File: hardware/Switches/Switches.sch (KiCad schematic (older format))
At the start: 22 parts, among them U101 MIC4604YM, U102 MIC4604YM

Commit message: snubber
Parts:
- added C105, C106, C107, C108: 100n, Capacitor_SMD:C_1210_3225Metric_Pad1.33x2.70mm_HandSolder, symbol Device:C_Small
- added R109, R110, R111, R112: 10, Resistor_SMD:R_1210_3225Metric_Pad1.30x2.65mm_HandSolder, symbol Device:R_Small_US
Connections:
- wire segments 71 -> 75
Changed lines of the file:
@@
 	5950 3950 5800 3950
 Wire Wire Line
-	6100 4350 5800 4350
-Wire Wire Line
-	3850 4350 4150 4350
+	6100 4350 5950 4350
+Wire Wire Line
+	3850 4350 4000 4350
 Wire Wire Line
 	5800 4350 4950 4350
@@
 Connection ~ 4150 4350
 Wire Wire Line
-	3850 2650 4150 2650
+	3850 2650 4000 2650
 Connection ~ 4150 2650
 Wire Wire Line
@@
 Connection ~ 5800 2650
 Wire Wire Line
-	5800 2650 6100 2650
+	5800 2650 5950 2650
 Wire Wire Line
 	4000 3550 4600 3550
@@
 Wire Wire Line
 	1400 4000 1400 4250
+$Comp
+L Device:R_Small_US R109
+U 1 1 606721D1
+P 4000 2750
+F 0 "R109" V 4050 2650 50  0000 C CNN
+F 1 "10" V 3800 2850 50  0000 C CNN
+F 2 "Resistor_SMD:R_1210_3225Metric_Pad1.30x2.65mm_HandSolder" H 4000 2750 50  0001 C CNN
+F 3 "~" H 4000 2750 50  0001 C CNN
+	1    4000 2750
+	1    0    0    1
+$EndComp
+Connection ~ 4000 2650
+Wire Wire Line
+	4000 2650 4150 2650
+$Comp
+L Device:C_Small C105
+U 1 1 606739D1
+P 4000 2950
+F 0 "C105" H 4092 2996 50  0000 L CNN
+F 1 "100n" H 4092 2905 50  0000 L CNN
+F 2 "Capacitor_SMD:C_1210_3225Metric_Pad1.33x2.70mm_HandSolder" H 4000 2950 50  0001 C CNN
+F 3 "~" H 4000 2950 50  0001 C CNN
+	1    4000 2950
+	1    0    0    -1
+$EndComp
+$Comp
+L Device:R_Small_US R111
+U 1 1 60674F65
+P 5950 2750
+F 0 "R111" V 6000 2650 50  0000 C CNN
+F 1 "10" V 5750 2850 50  0000 C CNN
+F 2 "Resistor_SMD:R_1210_3225Metric_Pad1.30x2.65mm_HandSolder" H 5950 2750 50  0001 C CNN
+F 3 "~" H 5950 2750 50  0001 C CNN
+	1    5950 2750
+	1    0    0    1
+$EndComp
+Connection ~ 5950 2650
+Wire Wire Line
+	5950 2650 6100 2650
+$Comp
+L Device:C_Small C107
+U 1 1 606754F2
+P 5950 2950
+F 0 "C107" H 6042 2996 50  0000 L CNN
+F 1 "100n" H 6042 2905 50  0000 L CNN
+F 2 "Capacitor_SMD:C_1210_3225Metric_Pad1.33x2.70mm_HandSolder" H 5950 2950 50  0001 C CNN
+F 3 "~" H 5950 2950 50  0001 C CNN
+	1    5950 2950
+	1    0    0    -1
+$EndComp
+$Comp
+L Device:R_Small_US R110
+U 1 1 6067713F
+P 4000 4050
+F 0 "R110" V 4050 3950 50  0000 C CNN
+F 1 "10" V 3800 4150 50  0000 C CNN
+F 2 "Resistor_SMD:R_1210_3225Metric_Pad1.30x2.65mm_HandSolder" H 4000 4050 50  0001 C CNN
+F 3 "~" H 4000 4050 50  0001 C CNN
+	1    4000 4050
+	1    0    0    1
+$EndComp
+$Comp
+L Device:C_Small C106
+U 1 1 6067937E
+P 4000 4250
+F 0 "C106" H 4092 4296 50  0000 L CNN
+F 1 "100n" H 4092 4205 50  0000 L CNN
+F 2 "Capacitor_SMD:C_1210_3225Metric_Pad1.33x2.70mm_HandSolder" H 4000 4250 50  0001 C CNN
+F 3 "~" H 4000 4250 50  0001 C CNN
+	1    4000 4250
+	1    0    0    -1
+$EndComp
+Connection ~ 4000 4350
+Wire Wire Line
+	4000 4350 4150 4350
+$Comp
+L Device:R_Small_US R112
+U 1 1 6067A27F
+P 5950 4050
+F 0 "R112" V 6000 3950 50  0000 C CNN
+F 1 "10" V 5750 4150 50  0000 C CNN
+F 2 "Resistor_SMD:R_1210_3225Metric_Pad1.30x2.65mm_HandSolder" H 5950 4050 50  0001 C CNN
+F 3 "~" H 5950 4050 50  0001 C CNN
+	1    5950 4050
+	1    0    0    1
+$EndComp
+$Comp
+L Device:C_Small C108
+U 1 1 6067A8BA
+P 5950 4250
+F 0 "C108" H 6042 4296 50  0000 L CNN
+F 1 "100n" H 6042 4205 50  0000 L CNN
+F 2 "Capacitor_SMD:C_1210_3225Metric_Pad1.33x2.70mm_HandSolder" H 5950 4250 50  0001 C CNN
+F 3 "~" H 5950 4250 50  0001 C CNN
+	1    5950 4250
+	1    0    0    -1
+$EndComp
+Connection ~ 5950 4350
+Wire Wire Line
+	5950 4350 5800 4350
 $EndSCHEMATC

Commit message: wip: switches pcb routed
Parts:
- removed C101, C104: 100n, Capacitor_SMD:C_0805_2012Metric_Pad1.18x1.45mm_HandSolder, symbol Device:C_Small
- removed C105: 100n, Capacitor_SMD:C_1210_3225Metric_Pad1.33x2.70mm_HandSolder, symbol Device:C_Small
- removed QH1_1, QH1_2, QH2_1, QH2_2, QL1_1, QL1_2, QL2_1, QL2_2: IAUT300N10S5N015, Package_TO_SOT_SMD:Infineon_PG-HSOF-8-1, symbol Device:Q_NMOS_GSD
- removed R109: 10, Resistor_SMD:R_1210_3225Metric_Pad1.30x2.65mm_HandSolder, symbol Device:R_Small_US
- removed U101, U102: MIC4604YM, Package_SO:SOIC-8_3.9x4.9mm_P1.27mm, symbol Driver_FET:MIC4604YM
- added C101, C104, C112, C113, C114, C115, C116, C117, C118, C119, C120, C121, C123, C124, C125, C126, C127, C128, C129, C130: 10u, Capacitor_SMD:C_1210_3225Metric_Pad1.33x2.70mm_HandSolder, symbol Device:C
- added C106: 100n, Capacitor_SMD:C_1210_3225Metric_Pad1.33x2.70mm_HandSolder, symbol Device:C_Small
- added C109, C110, C122: 10uF, Capacitor_SMD:C_1210_3225Metric_Pad1.33x2.70mm_HandSolder, symbol Device:C_Small
- added C111: 100nF, Capacitor_SMD:C_0805_2012Metric_Pad1.18x1.45mm_HandSolder, symbol Device:C_Small
- added C131, C132, C133: 1pF, Capacitor_SMD:C_0603_1608Metric_Pad1.08x0.95mm_HandSolder, symbol Device:C_Small
- added C134: 100nF, Capacitor_SMD:C_0603_1608Metric_Pad1.08x0.95mm_HandSolder, symbol Device:C_Small
- added J101, J102, J103, J104: BusBar, Switches:BusBar, symbol Connector:Conn_01x01_Male
- added J105: Conn_02x03_Odd_Even, Connector_PinHeader_1.27mm:PinHeader_2x10_P1.27mm_Vertical_SMD, symbol Connector_Generic:Conn_02x10_Odd_Even
- added Q101, Q102, Q103, Q104, Q105, Q106, Q107, Q108, Q109, Q110, Q111, Q112: IPT015N10N5, Package_TO_SOT_SMD:Infineon_PG-HSOF-8-1_ThermalVias, symbol Transistor_FET:IPT015N10N5
- added R110: 10, Resistor_SMD:R_1210_3225Metric_Pad1.30x2.65mm_HandSolder, symbol Device:R_Small_US
- added R113, R114, R115, R116: 4R7, Resistor_SMD:R_0805_2012Metric_Pad1.20x1.40mm_HandSolder, symbol Device:R_Small_US
- added R117: 47k, Resistor_SMD:R_0603_1608Metric_Pad0.98x0.95mm_HandSolder, symbol Device:R_Small_US
- added R118, R119, R120, R124, R125, R126, R127, R128, R129, R130, R131, R132, R133, R134, R135: 10k, Resistor_SMD:R_0603_1608Metric_Pad0.98x0.95mm_HandSolder, symbol Device:R_Small_US
- added R121, R122, R123: 330, Resistor_SMD:R_0603_1608Metric_Pad0.98x0.95mm_HandSolder, symbol Device:R_Small_US
- added TH101: SDNT2012X103F3950FTF, Resistor_SMD:R_0805_2012Metric_Pad1.20x1.40mm_HandSolder, symbol Device:Thermistor_NTC_US
- added U101, U102: UCC27211DDAR, Package_SO:SOIC-8-1EP_3.9x4.9mm_P1.27mm_EP2.514x3.2mm_ThermalVias, symbol ucc27211ddar:UCC27211DDAR
- C102, C103: footprint Capacitor_SMD:C_0805_2012Metric_Pad1.18x1.45mm_HandSolder -> Capacitor_SMD:C_1210_3225Metric_Pad1.33x2.70mm_HandSolder
- C107: value 100n -> 10uF
- C108: value 100n -> 100nF; footprint Capacitor_SMD:C_1210_3225Metric_Pad1.33x2.70mm_HandSolder -> Capacitor_SMD:C_0805_2012Metric_Pad1.18x1.45mm_HandSolder
- R101, R102: footprint Resistor_SMD:R_0805_2012Metric_Pad1.20x1.40mm_HandSolder -> Resistor_SMD:R_1210_3225Metric_Pad1.30x2.65mm_HandSolder
- R103, R104, R105, R106, R107, R108: value 10 -> 4R7
- R111, R112: value 10 -> 4R7; footprint Resistor_SMD:R_1210_3225Metric_Pad1.30x2.65mm_HandSolder -> Resistor_SMD:R_0805_2012Metric_Pad1.20x1.40mm_HandSolder
- renumbered C106 to C105, R110 to R109
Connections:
- net labels added: +15V, +BATT, GH1_3, GH2_3, GL1_3, GL3_3, GNDA, PWM_H1, PWM_H2, PWM_L1, PWM_L2, SL1_sen, SL2_sen, TEMP1, Vin_sen
- net labels removed: VCC, Vin
- wire segments 75 -> 325
- no-connect marks 0 -> 6
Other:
- note added: "References:\nhttps://www.ti.com/lit/an/slva959a/slva959a.pdf\nhttps://www.ti.com/tool/TIDA-00774"
- note added: "TODO:\n [_] Definir fixação no dissipador!!!!!!!!\n [_] Calcular capacitores do Driver!\n [x] Incluir sensores de tensão\n [x] Incluir sensores de temperatura\n [_] Incluir diodo no Snubber\n [_] Usar plano em baixo da barra de cobre para aumentar a capacitância de entrada\n [_] Verificar pinagem no conector do controle\n [_] Calcular capacitores de entrada\n [x] Incluir sensores de corrente -> S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"
- note added: "≃12kHz"
- note added: "≃200Hz@25°C\n≃2.7kHz@125°C"
- note removed: "Q1-Q8 IAUT300N10S5N015"
- moved on the sheet: C105, R109

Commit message: Driver and MOSFETs protections added, driver calculations done.
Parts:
- added C135, C136, C137, C138, C139, C140, C141, C142, C143, C144, C145, C146, C147, C148, C149, C150, C151, C152, C153, C154: 100n, Capacitor_SMD:C_0805_2012Metric_Pad1.18x1.45mm_HandSolder, symbol Device:C
- added C155, C156, C157, C158, C159, C160, C161, C162, C163, C164, C165, C166, C167, C168, C169, C170, C171, C172, C173, C174: 10n, Capacitor_SMD:C_0603_1608Metric_Pad1.08x0.95mm_HandSolder, symbol Device:C
- added C175, C176, C177, C178, C179, C180, C181, C182, C183, C184, C185, C186, C187, C188, C189, C190, C191, C192, C193, C194: 1n, Capacitor_SMD:C_0603_1608Metric_Pad1.08x0.95mm_HandSolder, symbol Device:C
- added C195, C196: 1n, Capacitor_SMD:C_0603_1608Metric_Pad1.08x0.95mm_HandSolder, symbol Device:C_Small
- added D101, D103, D104, D105, D106, D107, D108, D109, D111, D112, D113, D115, D116, D117: B0530W, Diode_SMD:D_SOD-123F, symbol Device:D_Schottky_Small
- added D102, D110: MBR2H100SFT3G, Diode_SMD:D_SOD-123F, symbol Device:D_Schottky_Small
- added D114, D118: MM3Z15V, Diode_SMD:D_SOD-323, symbol Device:D_Zener_Small
- added R136, R137: 2R, Resistor_SMD:R_0603_1608Metric_Pad0.98x0.95mm_HandSolder, symbol Device:R_Small_US
- C107, C110: value 10uF -> 10u
- C108, C111, C134: value 100nF -> 100n
- C109, C122: value 10uF -> 4.7u
- C131, C132, C133: value 1pF -> 1p
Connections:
- wire segments 325 -> 617
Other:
- note added: "TODO:\n [_] Definir fixação no dissipador!!!!!!!!\n [x] Calcular capacitores do Driver!\n [x] Incluir sensores de tensão\n [x] Incluir sensores de temperatura\n [_] Incluir diodo no Snubber\n [_] Usar plano em baixo da barra de cobre para aumentar a capacitância de entrada\n [_] Verificar pinagem no conector do controle\n [_] Calcular capacitores de entrada\n [x] Incluir sensores de corrente -> S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"
- note removed: "TODO:\n [_] Definir fixação no dissipador!!!!!!!!\n [_] Calcular capacitores do Driver!\n [x] Incluir sensores de tensão\n [x] Incluir sensores de temperatura\n [_] Incluir diodo no Snubber\n [_] Usar plano em baixo da barra de cobre para aumentar a capacitância de entrada\n [_] Verificar pinagem no conector do controle\n [_] Calcular capacitores de entrada\n [x] Incluir sensores de corrente -> S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"
- moved on the sheet: C101, C102, C103, C104, C105, C106, C107, C108, C109, C110, C111, C112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

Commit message: wip: PCB updated
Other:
- note added: "References:\nhttps://www.ti.com/lit/an/slva959a/slva959a.pdf\nhttps://www.ti.com/tool/TIDA-00774\nhttps://www.ti.com/lit/ug/tiducb6/tiducb6.pdf"
- note removed: "References:\nhttps://www.ti.com/lit/an/slva959a/slva959a.pdf\nhttps://www.ti.com/tool/TIDA-00774"

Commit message: Updating Switches PCB
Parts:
- R117: value 47k -> 5k6
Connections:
- net labels added: +5VA
- wire segments 617 -> 624
- no-connect marks 6 -> 0
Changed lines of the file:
@@
 	0    1    1    0
 $EndComp
-Text Label 3150 2550 0    50   ~ 0
+Text Label 3150 2650 0    50   ~ 0
 PWM_H1
-Text Label 3150 2450 0    50   ~ 0
+Text Label 3150 2550 0    50   ~ 0
 PWM_L1
-Text Label 3150 2750 0    50   ~ 0
+Text Label 3150 2850 0    50   ~ 0
 PWM_H2
-Text Label 3150 2650 0    50   ~ 0
+Text Label 3150 2750 0    50   ~ 0
 PWM_L2
 $Comp
 L power:+15V #PWR0101
 U 1 1 60920038
-P 3150 1600
-F 0 "#PWR0101" H 3150 1450 50  0001 C CNN
-F 1 "+15V" H 3150 1800 50  0000 C CNN
-F 2 "" H 3150 1600 50  0001 C CNN
-F 3 "" H 3150 1600 50  0001 C CNN
-	1    3150 1600
+P 4100 2000
+F 0 "#PWR0101" H 4100 1850 50  0001 C CNN
+F 1 "+15V" H 4100 2200 50  0000 C CNN
+F 2 "" H 4100 2000 50  0001 C CNN
+F 3 "" H 4100 2000 50  0001 C CNN
+	1    4100 2000
 	1    0    0    -1
 $EndComp
 Wire Wire Line
-	3150 1600 3150 1650
+	4100 2000 4100 2050
 Wire Wire Line
 	3150 2050 3050 2050
-Connection ~ 3150 1650
-Wire Wire Line
-	3150 1650 3150 2050
 $Comp
 L Device:C_Small C111
@@
 L power:PWR_FLAG #FLG0101
 U 1 1 60CF3365
-P 2800 1650
-F 0 "#FLG0101" H 2800 1725 50  0001 C CNN
-F 1 "PWR_FLAG" H 2800 1850 50  0000 C CNN
-F 2 "" H 2800 1650 50  0001 C CNN
-F 3 "~" H 2800 1650 50  0001 C CNN
-	1    2800 1650
+P 3750 2050
+F 0 "#FLG0101" H 3750 2125 50  0001 C CNN
+F 1 "PWR_FLAG" H 3750 2250 50  0000 C CNN
+F 2 "" H 3750 2050 50  0001 C CNN
+F 3 "~" H 3750 2050 50  0001 C CNN
+	1    3750 2050
 	1    0    0    -1
 $EndComp
 Wire Wire Line
-	2800 1650 3150 1650
-NoConn ~ 2450 2250
-NoConn ~ 2450 2350
-NoConn ~ 3150 2350
-NoConn ~ 3150 2850
-NoConn ~ 3150 2950
-NoConn ~ 3150 2250
+	3750 2050 4100 2050
 Wire Wire Line
 	3150 2850 3050 2850
 Wire Wire Line
-	3150 2950 3050 2950
-Wire Wire Line
 	1500 8200 1500 8000
 Wire Wire Line
@@
 Text Notes 9550 11050 0    50   ~ 0
 References:\nhttps://www.ti.com/lit/an/slva959a/slva959a.pdf\nhttps://www.ti.com/tool/TIDA-00774\nhttps://www.ti.com/lit/ug/tiducb6/tiducb6.pdf
-Text Label 2450 2750 2    50   ~ 0
+Text Label 2450 2850 2    50   ~ 0
 TEMP1
 $Comp
@@
 Wire Wire Line
 	7950 2150 7950 2250
-Text Label 2450 2450 2    50   ~ 0
-SL1_sen
 Text Label 2450 2550 2    50   ~ 0
-SL2_sen
+SL1_sen
 Text Label 2450 2650 2    50   ~ 0
+SL2_sen
+Text Label 2450 2750 2    50   ~ 0
 Vin_sen
 $Comp
@@
 P 9600 2350
 F 0 "R117" H 9450 2400 50  0000 C CNN
-F 1 "47k" H 9450 2300 50  0000 C CNN
+F 1 "5k6" H 9450 2300 50  0000 C CNN
 F 2 "Resistor_SMD:R_0603_1608Metric_Pad0.98x0.95mm_HandSolder" H 9600 2350 50  0001 C CNN
 F 3 "~" H 9600 2350 50  0001 C CNN
@@
 	-1   0    0    -1
 $EndComp
-$Comp
-L power:+15V #PWR0113
-U 1 1 60A6701F
-P 9600 2250
-F 0 "#PWR0113" H 9600 2100 50  0001 C CNN
-F 1 "+15V" H 9600 2450 50  0000 C CNN
-F 2 "" H 9600 2250 50  0001 C CNN
-F 3 "" H 9600 2250 50  0001 C CNN
-	1    9600 2250
-	1    0    0    -1
-$EndComp
 Wire Wire Line
 	9600 2500 9600 2550
@@
 $EndComp
 Wire Wire Line
-	1950 2850 1950 2950
-Wire Wire Line
-	1950 2850 2550 2850
-Wire Wire Line
 	1950 2950 2550 2950
 Connection ~ 1950 2950
@@
 Wire Wire Line
 	3150 2150 3150 2050
-Connection ~ 3150 2050
 $Comp
 L power:PWR_FLAG #FLG0104
 U 1 1 6142A2F3
-P 1950 2850
-F 0 "#FLG0104" H 1950 2925 50  0001 C CNN
-F 1 "PWR_FLAG" H 1950 3050 50  0000 C CNN
-F 2 "" H 1950 2850 50  0001 C CNN
-F 3 "~" H 1950 2850 50  0001 C CNN
-	1    1950 2850
+P 1950 2950
+F 0 "#FLG0104" H 1950 3025 50  0001 C CNN
+F 1 "PWR_FLAG" H 1950 3150 50  0000 C CNN
+F 2 "" H 1950 2950 50  0001 C CNN
+F 3 "~" H 1950 2950 50  0001 C CNN
+	1    1950 2950
 	1    0    0    -1
 $EndComp
-Connection ~ 1950 2850
 Wire Wire Line
 	2450 2050 1950 2050
@@
 	1    0    0    -1
 $EndComp
+$Comp
+L power:PWR_FLAG #FLG0105
+U 1 1 6079DC9E
+P 3750 2950
+F 0 "#FLG0105" H 3750 3025 50  0001 C CNN
+F 1 "PWR_FLAG" H 3750 3150 50  0000 C CNN
+F 2 "" H 3750 2950 50  0001 C CNN
+F 3 "~" H 3750 2950 50  0001 C CNN
+	1    3750 2950
+	1    0    0    -1
+$EndComp
+Wire Wire Line
+	3050 2950 3750 2950
+Wire Wire Line
+	4100 2950 3750 2950
+Connection ~ 3750 2950
+Wire Wire Line
+	2550 2850 2450 2850
+Wire Wire Line
+	2450 2150 2450 2250
+Connection ~ 2450 2150
+Connection ~ 2450 2250
+Wire Wire Line
+	2450 2250 2450 2350
+Connection ~ 2450 2350
+Wire Wire Line
+	2450 2350 2450 2450
+Wire Wire Line
+	3150 2150 3150 2250
+Connection ~ 3150 2150
+Connection ~ 3150 2250
+Wire Wire Line
+	3150 2250 3150 2350
+Connection ~ 3150 2350
+Wire Wire Line
+	3150 2350 3150 2450
+$Comp
+L power:+5VA #PWR0113
+U 1 1 60BF436C
+P 9600 2250
+F 0 "#PWR0113" H 9600 2100 50  0001 C CNN
+F 1 "+5VA" H 9650 2450 50  0000 C CNN
+F 2 "" H 9600 2250 50  0001 C CNN
+F 3 "" H 9600 2250 50  0001 C CNN
+	1    9600 2250
+	1    0    0    -1
+$EndComp
+Wire Wire Line
+	3750 2050 3150 2050
+Connection ~ 3750 2050
+Connection ~ 3150 2050
+Wire Wire Line
+	4100 2900 4100 2950
+$Comp
+L power:+5VA #PWR0139
+U 1 1 60BF364D
+P 4100 2900
+F 0 "#PWR0139" H 4100 2750 50  0001 C CNN
+F 1 "+5VA" H 4150 3100 50  0000 C CNN
+F 2 "" H 4100 2900 50  0001 C CNN
+F 3 "" H 4100 2900 50  0001 C CNN
+	1    4100 2900
+	1    0    0    -1
+$EndComp

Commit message: PCB updated, not yet finished
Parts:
- removed C101, C104, C112, C113, C114, C115, C116, C117, C118, C119, C120, C121, C123, C124, C125, C126, C127, C128, C129, C130: 10u, Capacitor_SMD:C_1210_3225Metric_Pad1.33x2.70mm_HandSolder, symbol Device:C
- removed C135, C136, C137, C138, C139, C140, C141, C142, C143, C144, C145, C146, C147, C148, C149, C150, C151, C152, C153, C154: 100n, Capacitor_SMD:C_0805_2012Metric_Pad1.18x1.45mm_HandSolder, symbol Device:C
- removed C155, C156, C157, C158, C159, C160, C161, C162, C163, C164, C165, C166, C167, C168, C169, C170, C171, C172, C173, C174: 10n, Capacitor_SMD:C_0603_1608Metric_Pad1.08x0.95mm_HandSolder, symbol Device:C
- removed C175, C176, C177, C178, C179, C180, C181, C182, C183, C184, C185, C186, C187, C188, C189, C190, C191, C192, C193, C194: 1n, Capacitor_SMD:C_0603_1608Metric_Pad1.08x0.95mm_HandSolder, symbol Device:C
- C131, C132, C133: value 1p -> 1n
- J101, J102: footprint Switches:BusBar -> Switches:BusBar1
- J103, J104: footprint Switches:BusBar -> Switches:BusBar2
- Q101, Q102, Q103, Q104, Q105, Q106, Q107, Q108, Q109, Q110, Q111, Q112: footprint Package_TO_SOT_SMD:Infineon_PG-HSOF-8-1_ThermalVias -> Switches:Infineon_PG-HSOF-8-1_ThermalVias_custom
- R122, R123: value 330 -> 3k3
- U101, U102: footprint Package_SO:SOIC-8-1EP_3.9x4.9mm_P1.27mm_EP2.514x3.2mm_ThermalVias -> Switches:SOIC-8-1EP_3.9x4.9mm_P1.27mm_EP2.514x3.2mm_ThermalVias
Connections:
- wire segments 624 -> 303
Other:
- note removed: "≃12kHz"

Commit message: Done, not yet checked
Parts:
- removed C102, C105, C106: 100n, Capacitor_SMD:C_1210_3225Metric_Pad1.33x2.70mm_HandSolder, symbol Device:C_Small
- removed R101, R109, R110: 10, Resistor_SMD:R_1210_3225Metric_Pad1.30x2.65mm_HandSolder, symbol Device:R_Small_US
- added Csn101, Csn105, Csn107: 100n, Capacitor_SMD:C_1210_3225Metric_Pad1.33x2.70mm_HandSolder, symbol Device:C_Small
- added Csn102, Csn104, Csn106, Csn108: NC, Capacitor_SMD:C_1210_3225Metric_Pad1.33x2.70mm_HandSolder, symbol Device:C_Small
- added Dsn101, Dsn103, Dsn105, Dsn107: MBR2H100SFT3G, Diode_SMD:D_SOD-123F, symbol Device:D_Schottky_Small
- added Dsn102, Dsn104, Dsn106, Dsn108: NC, Diode_SMD:D_SOD-123F, symbol Device:D_Schottky_Small
- added Rsn101, Rsn105, Rsn107: 10, Resistor_SMD:R_1210_3225Metric_Pad1.30x2.65mm_HandSolder, symbol Device:R_Small_US
- added Rsn102, Rsn104, Rsn106, Rsn108: NC, Resistor_SMD:R_1210_3225Metric_Pad1.30x2.65mm_HandSolder, symbol Device:R_Small_US
- Q101, Q102, Q103, Q104, Q105, Q106, Q107, Q108, Q109, Q110, Q111, Q112: footprint Switches:Infineon_PG-HSOF-8-1_ThermalVias_custom -> Switches:Infineon_PG-HSOF-8-1_ThermalVias3
- renumbered C103 to Csn103, R102 to Rsn103
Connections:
- net +BATT: now also Dsn101.2 (A), Dsn102.2 (A), Dsn103.2 (A), Dsn104.2 (A), Rsn101.1, Rsn102.1, Rsn104.1
- net GND: now also Csn105.2, Csn106.2, Csn107.2, Csn108.2
- net SL1: now also Csn101.2, Csn102.2, Dsn105.2 (A), Dsn106.2 (A), Rsn105.1, Rsn106.1
- net SL2: now also Csn104.2, Dsn107.2 (A), Dsn108.2 (A), Rsn107.1, Rsn108.1
- net at Csn103.1, Rsn103.2: now also Csn104.1, Dsn103.1 (K), Dsn104.1 (K), Rsn104.2
- new net: Csn107.1, Csn108.1, Dsn107.1 (K), Dsn108.1 (K), Rsn107.2, Rsn108.2
- new net: Csn105.1, Csn106.1, Dsn105.1 (K), Dsn106.1 (K), Rsn105.2, Rsn106.2
- new net: Csn101.1, Csn102.1, Dsn101.1 (K), Dsn102.1 (K), Rsn101.2, Rsn102.2

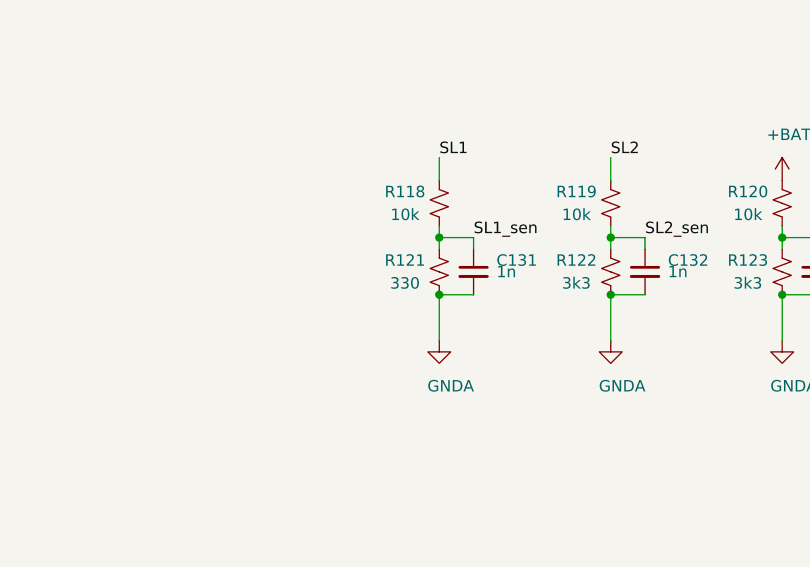
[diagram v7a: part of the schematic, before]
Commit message: small changes (compnents values)
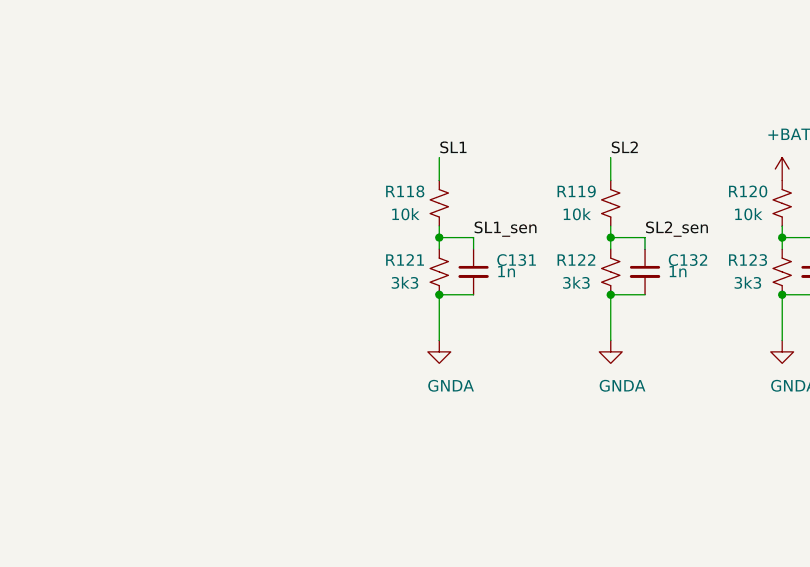
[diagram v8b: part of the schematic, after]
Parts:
- R121: value 330 -> 3k3
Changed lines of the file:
@@
 P 7200 2650
 F 0 "R121" H 7050 2700 50  0000 C CNN
-F 1 "330" H 7050 2600 50  0000 C CNN
+F 1 "3k3" H 7050 2600 50  0000 C CNN
 F 2 "Resistor_SMD:R_0603_1608Metric_Pad0.98x0.95mm_HandSolder" H 7200 2650 50  0001 C CNN
 F 3 "~" H 7200 2650 50  0001 C CNN
